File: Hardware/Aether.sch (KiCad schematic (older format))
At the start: 13 parts, among them J1 PRGM, J2 CONN-2, J3 CONN-2, J4 CONN-2, J5 CONN-2, J6 CONN-3, J7 CONN-3

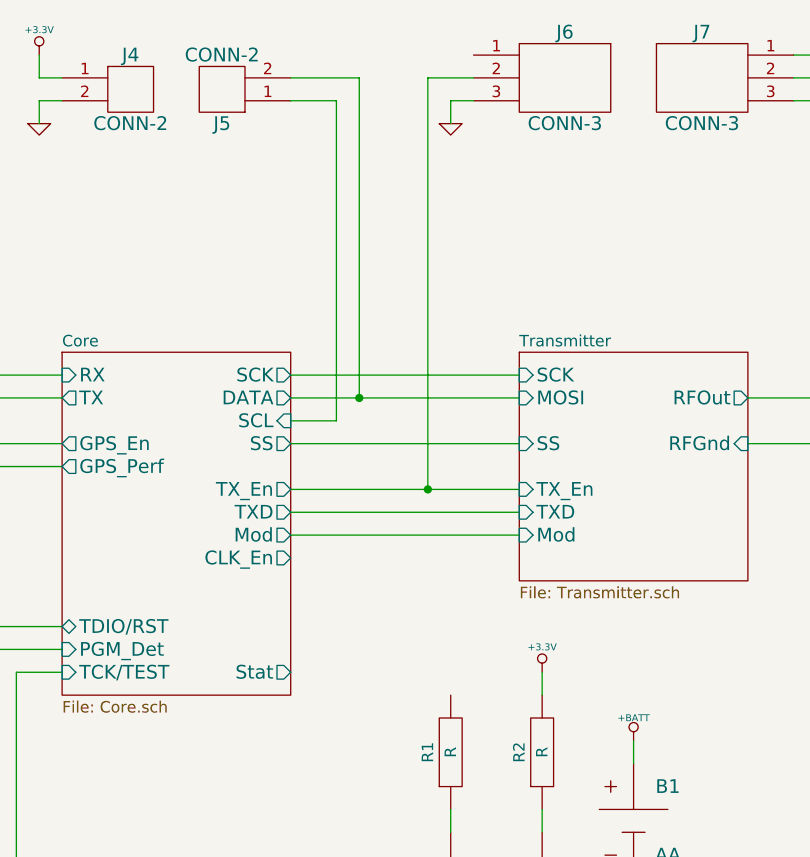
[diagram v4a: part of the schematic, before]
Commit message: Change to soft SPI, routing
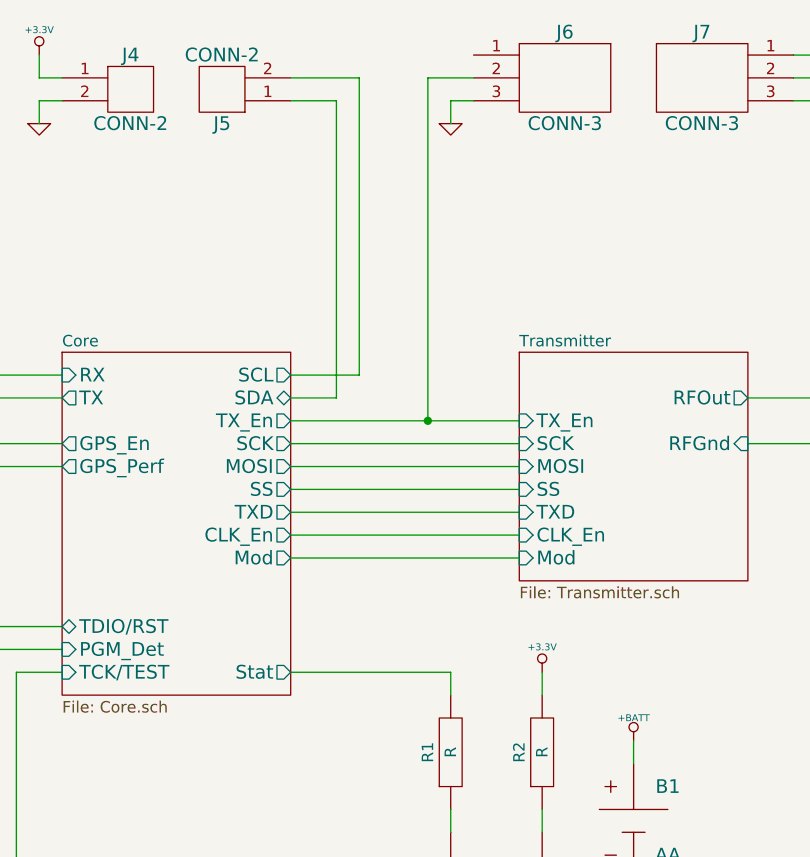
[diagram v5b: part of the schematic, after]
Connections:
- net Core/DATA is gone; now on net Core/SCL: J5.2
- net Core/SCL: no longer J5.1
- net Core/Stat: now also R1.2
- new net Core/SDA: J5.1
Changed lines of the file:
@@
 F2 "RFOut" O R 8200 3500 60
 F3 "RFGnd" I R 8200 3700 60
-F4 "SCK" I L 7200 3400 60
-F5 "MOSI" I L 7200 3500 60
-F6 "SS" I L 7200 3700 60
-F7 "TX_En" I L 7200 3900 60
+F4 "SCK" I L 7200 3700 60
+F5 "MOSI" I L 7200 3800 60
+F6 "SS" I L 7200 3900 60
+F7 "TX_En" I L 7200 3600 60
 F8 "TXD" I L 7200 4000 60
-F9 "Mod" I L 7200 4100 60
+F9 "Mod" I L 7200 4200 60
+F10 "CLK_En" I L 7200 4100 60
 $EndSheet
 $Comp
@@
 	8900 3900 9000 3900
 Connection ~ 8900 3800
-Wire Wire Line
-	6200 3400 7200 3400
-Wire Wire Line
-	6200 3500 7200 3500
-Wire Wire Line
-	6200 3700 7200 3700
 Wire Wire Line
 	4200 3400 5200 3400
@@
 Wire Wire Line
 	5200 3800 4200 3800
-Wire Wire Line
-	6200 3900 7200 3900
-Wire Wire Line
-	6200 4000 7200 4000
-Wire Wire Line
-	6200 4100 7200 4100
 $Comp
 L R R2
@@
 F3 "TX" O L 5200 3500 60
 F4 "GPS_En" O L 5200 3700 60
-F5 "SCK" O R 6200 3400 60
-F6 "SS" O R 6200 3700 60
-F7 "TX_En" O R 6200 3900 60
-F8 "TXD" O R 6200 4000 60
-F9 "Mod" O R 6200 4100 60
-F10 "TDIO/RST" B L 5200 4500 60
-F11 "TCK/TEST" I L 5200 4700 60
-F12 "PGM_Det" I L 5200 4600 60
-F13 "GPS_Perf" O L 5200 3800 60
-F14 "DATA" O R 6200 3500 60
-F15 "SCL" I R 6200 3600 60
-F16 "Stat" O R 6200 4700 60
-F17 "CLK_En" O R 6200 4200 60
+F5 "TDIO/RST" B L 5200 4500 60
+F6 "TCK/TEST" I L 5200 4700 60
+F7 "PGM_Det" I L 5200 4600 60
+F8 "GPS_Perf" O L 5200 3800 60
+F9 "Stat" O R 6200 4700 60
+F10 "SDA" B R 6200 3500 60
+F11 "SCL" O R 6200 3400 60
+F12 "SCK" O R 6200 3700 60
+F13 "SS" O R 6200 3900 60
+F14 "TX_En" O R 6200 3600 60
+F15 "TXD" O R 6200 4000 60
+F16 "Mod" O R 6200 4200 60
+F17 "CLK_En" O R 6200 4100 60
+F18 "MOSI" O R 6200 3800 60
 $EndSheet
 $Comp
@@
 	6200 2200 6400 2200
 Wire Wire Line
-	6400 2200 6400 3600
-Wire Wire Line
-	6400 3600 6200 3600
-Wire Wire Line
 	6200 2100 6500 2100
-Wire Wire Line
-	6500 2100 6500 3500
-Connection ~ 6500 3500
 $Comp
 L GND #PWR08
@@
 	7000 2100 6800 2100
 Wire Wire Line
-	6800 2100 6800 3900
-Connection ~ 6800 3900
+	6200 4700 6900 4700
+Wire Wire Line
+	6900 4700 6900 4800
+Wire Wire Line
+	6200 3400 6500 3400
+Wire Wire Line
+	6500 3400 6500 2100
+Wire Wire Line
+	6200 3500 6400 3500
+Wire Wire Line
+	6400 3500 6400 2200
+Wire Wire Line
+	6200 3600 7200 3600
+Wire Wire Line
+	6200 3700 7200 3700
+Wire Wire Line
+	6200 3800 7200 3800
+Wire Wire Line
+	6200 3900 7200 3900
+Wire Wire Line
+	6200 4000 7200 4000
+Wire Wire Line
+	6200 4100 7200 4100
+Wire Wire Line
+	6200 4200 7200 4200
+Wire Wire Line
+	6800 2100 6800 3600
+Connection ~ 6800 3600
 $EndSCHEMATC

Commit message: Optimize some values
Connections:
- net +BATT: now also J2.1, J6.1
- net GND: now also J2.2
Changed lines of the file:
@@
 	6800 2100 6800 3600
 Connection ~ 6800 3600
+$Comp
+L +BATT #PWR011
+U 1 1 52F2F27B
+P 6900 1900
+F 0 "#PWR011" H 6900 1850 20  0001 C CNN
+F 1 "+BATT" H 6900 2000 30  0000 C CNN
+F 2 "" H 6900 1900 60  0000 C CNN
+F 3 "" H 6900 1900 60  0000 C CNN
+	1    6900 1900
+	1    0    0    -1
+$EndComp
+Wire Wire Line
+	6900 1900 6900 2000
+Wire Wire Line
+	6900 2000 7000 2000
+$Comp
+L +BATT #PWR012
+U 1 1 52F2F5FA
+P 3100 2000
+F 0 "#PWR012" H 3100 1950 20  0001 C CNN
+F 1 "+BATT" H 3100 2100 30  0000 C CNN
+F 2 "" H 3100 2000 60  0000 C CNN
+F 3 "" H 3100 2000 60  0000 C CNN
+	1    3100 2000
+	1    0    0    -1
+$EndComp
+$Comp
+L GND #PWR013
+U 1 1 52F2F609
+P 3100 2300
+F 0 "#PWR013" H 3100 2300 30  0001 C CNN
+F 1 "GND" H 3100 2230 30  0001 C CNN
+F 2 "" H 3100 2300 60  0000 C CNN
+F 3 "" H 3100 2300 60  0000 C CNN
+	1    3100 2300
+	1    0    0    -1
+$EndComp
+Wire Wire Line
+	3100 2300 3100 2200
+Wire Wire Line
+	3100 2200 3200 2200
+Wire Wire Line
+	3100 2000 3100 2100
+Wire Wire Line
+	3100 2100 3200 2100
 $EndSCHEMATC
